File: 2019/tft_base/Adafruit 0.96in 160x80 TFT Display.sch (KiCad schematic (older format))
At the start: 14 parts, among them CN1 MICROSD, IC5 APX803, Q1 MMBT2222, U2 MIC5225-3.3, U3 74HC4050D

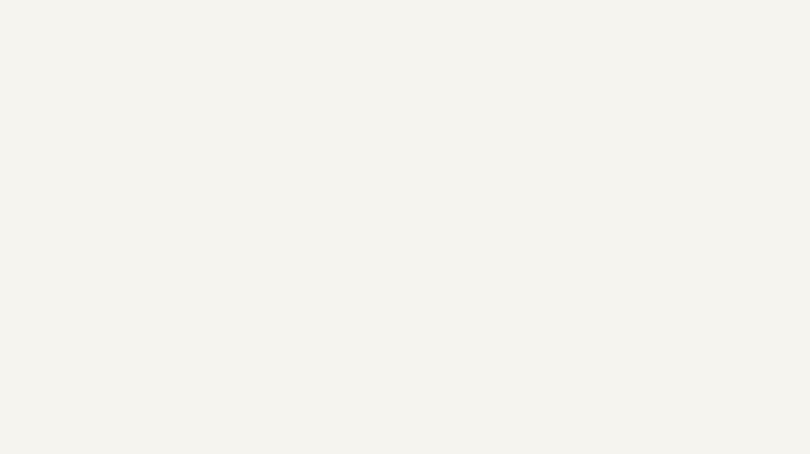
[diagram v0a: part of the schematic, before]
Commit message: Add Flash Breakout
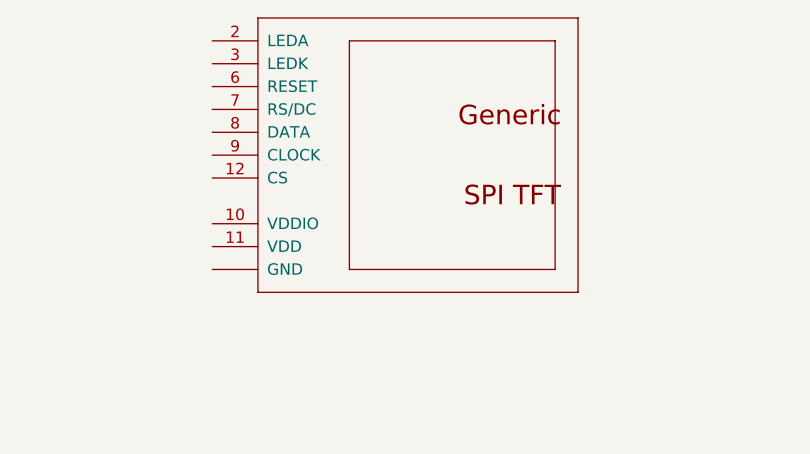
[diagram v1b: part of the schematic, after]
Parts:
- added ?: DISP_LCD_0.9IN_160X80, symbol Adafruit_0.96in_160x80_TFT_Display-eagle-import:DISP_LCD_0.9IN_160X80
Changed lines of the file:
@@
 Wire Wire Line
 	5625 21950 5625 22050
+$Comp
+L Adafruit_0.96in_160x80_TFT_Display-eagle-import:DISP_LCD_0.9IN_160X80 ?
+U 1 1 5CCE3E72
+P 5550 3625
+F 0 "?" H 5600 3675 50  0001 C CNN
+F 1 "DISP_LCD_0.9IN_160X80" H 5550 3625 50  0001 C CNN
+F 2 "" H 5550 3625 50  0001 C CNN
+F 3 "" H 5550 3625 50  0001 C CNN
+	1    5550 3625
+	1    0    0    -1
+$EndComp
 $EndSCHEMATC
